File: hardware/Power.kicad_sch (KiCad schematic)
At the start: 0 parts

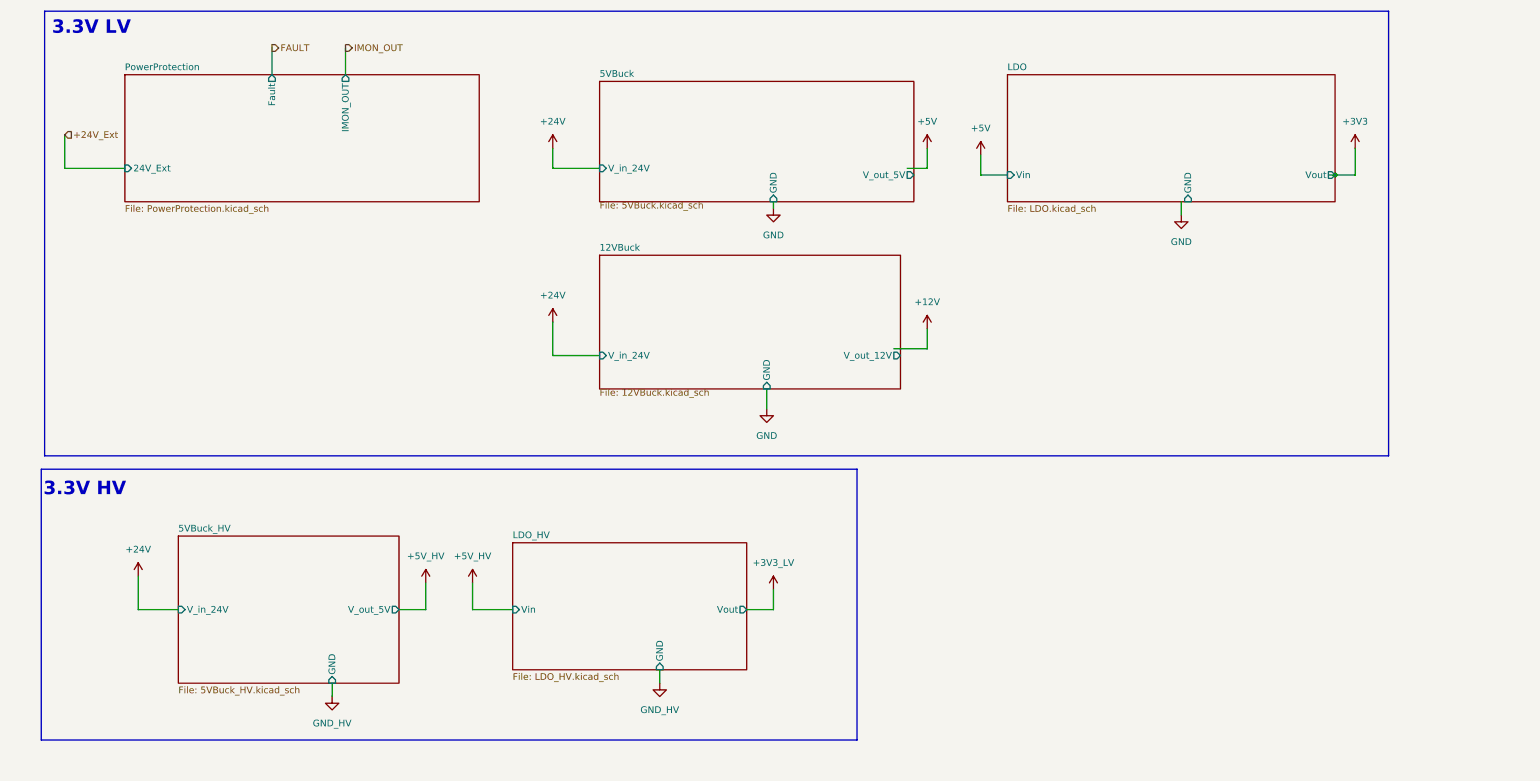
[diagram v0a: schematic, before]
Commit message: added designs for LZSR-80P and AMC class voltage sense
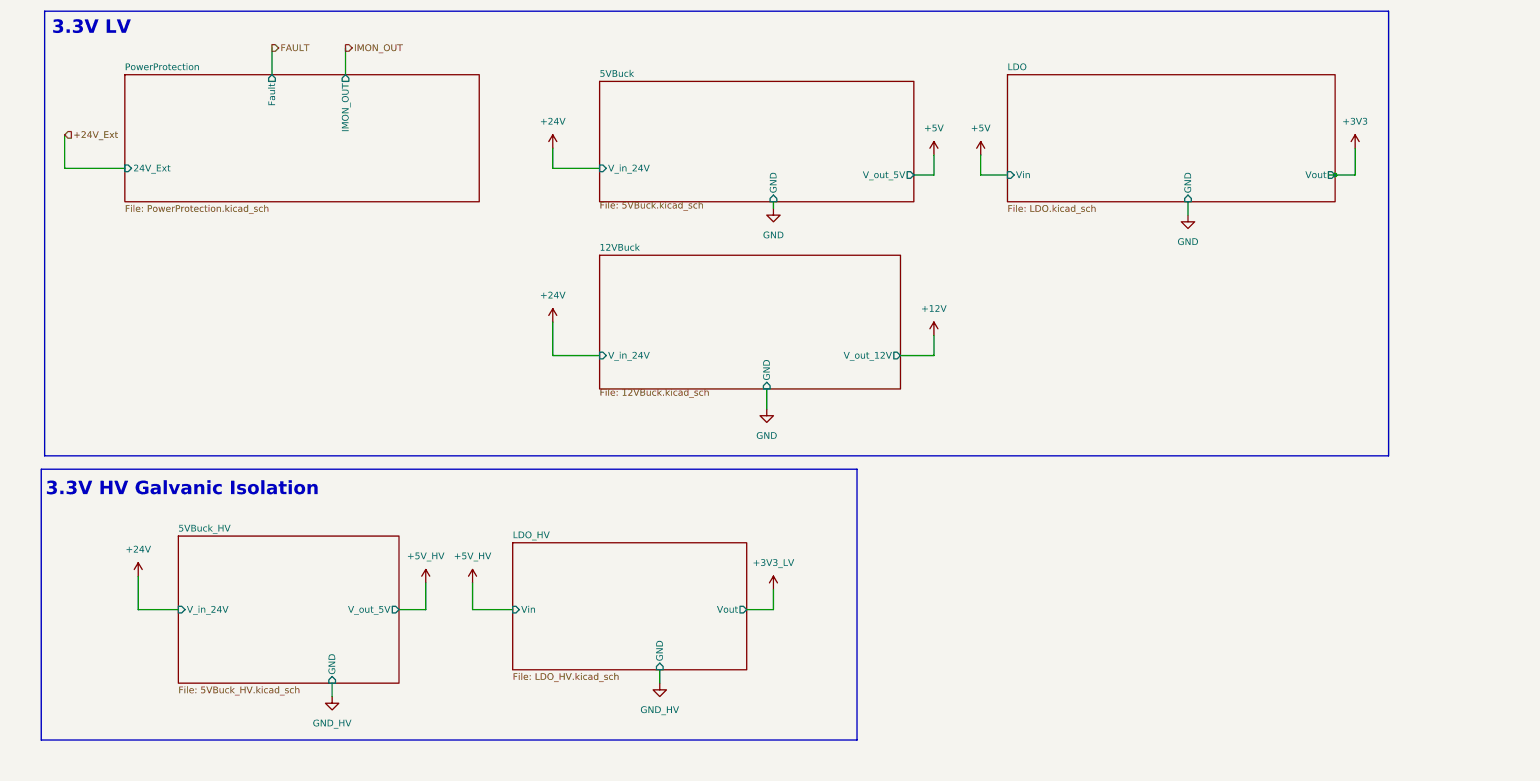
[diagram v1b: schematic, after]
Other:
- note added: "3.3V HV Galvanic Isolation"
- note removed: "3.3V HV"
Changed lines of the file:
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@@
 		)
 	)
-	(text "3.3V HV"
-		(exclude_from_sim no)
-		(at 26.67 109.22 0)
+	(text "3.3V HV Galvanic Isolation\n"
+		(exclude_from_sim no)
+		(at 45.212 109.22 0)
 		(effects
 			(font
@@
 	(wire
 		(pts
-			(xy 180.34 82.55) (xy 186.69 82.55)
+			(xy 181.61 83.82) (xy 187.96 83.82)
 		)
 		(stroke
@@
 	(wire
 		(pts
-			(xy 234.95 57.15) (xy 234.95 54.61)
+			(xy 236.22 57.15) (xy 236.22 54.61)
 		)
 		(stroke
@@
 	(wire
 		(pts
-			(xy 186.69 44.45) (xy 186.69 48.26)
+			(xy 187.96 45.72) (xy 187.96 49.53)
 		)
 		(stroke
@@
 	(wire
 		(pts
-			(xy 186.69 78.74) (xy 186.69 82.55)
+			(xy 187.96 80.01) (xy 187.96 83.82)
 		)
 		(stroke
@@
 	(wire
 		(pts
-			(xy 182.88 48.26) (xy 186.69 48.26)
+			(xy 184.15 49.53) (xy 187.96 49.53)
 		)
 		(stroke
@@
 	(symbol
 		(lib_id "power:+12V")
-		(at 186.69 78.74 0)
+		(at 187.96 80.01 0)
 		(unit 1)
 		(exclude_from_sim no)
@@
 		(fields_autoplaced yes)
 		(property "Reference" "#PWR07"
-			(at 186.69 82.55 0)
+			(at 187.96 83.82 0)
 			(effects
 				(font
@@
 		)
 		(property "Value" "+12V"
-			(at 186.69 73.66 0)
-			(effects
-				(font
-					(size 1.27 1.27)
-				)
-			)
-		)
-		(property "Footprint" ""
-			(at 186.69 78.74 0)
-			(effects
-				(font
-					(size 1.27 1.27)
-				)
-				(hide yes)
-			)
-		)
-		(property "Datasheet" ""
-			(at 186.69 78.74 0)
+			(at 187.96 74.93 0)
+			(effects
+				(font
+					(size 1.27 1.27)
+				)
+			)
+		)
+		(property "Footprint" ""
+			(at 187.96 80.01 0)
+			(effects
+				(font
+					(size 1.27 1.27)
+				)
+				(hide yes)
+			)
+		)
+		(property "Datasheet" ""
+			(at 187.96 80.01 0)
 			(effects
 				(font
@@
 		)
 		(property "Description" "Power symbol creates a global label with name \"+12V\""
-			(at 186.69 78.74 0)
+			(at 187.96 80.01 0)
 			(effects
 				(font
@@
 	(symbol
 		(lib_id "power:+5V")
-		(at 186.69 44.45 0)
+		(at 187.96 45.72 0)
 		(unit 1)
 		(exclude_from_sim no)
@@
 		(fields_autoplaced yes)
 		(property "Reference" "#PWR08"
-			(at 186.69 48.26 0)
+			(at 187.96 49.53 0)
 			(effects
 				(font
@@
 		)
 		(property "Value" "+5V"
-			(at 186.69 39.37 0)
-			(effects
-				(font
-					(size 1.27 1.27)
-				)
-			)
-		)
-		(property "Footprint" ""
-			(at 186.69 44.45 0)
-			(effects
-				(font
-					(size 1.27 1.27)
-				)
-				(hide yes)
-			)
-		)
-		(property "Datasheet" ""
-			(at 186.69 44.45 0)
+			(at 187.96 40.64 0)
+			(effects
+				(font
+					(size 1.27 1.27)
+				)
+			)
+		)
+		(property "Footprint" ""
+			(at 187.96 45.72 0)
+			(effects
+				(font
+					(size 1.27 1.27)
+				)
+				(hide yes)
+			)
+		)
+		(property "Datasheet" ""
+			(at 187.96 45.72 0)
 			(effects
 				(font
@@
 		)
 		(property "Description" "Power symbol creates a global label with name \"+5V\""
-			(at 186.69 44.45 0)
+			(at 187.96 45.72 0)
 			(effects
 				(font
@@
 	(symbol
 		(lib_id "power:GND")
-		(at 234.95 57.15 0)
+		(at 236.22 57.15 0)
 		(unit 1)
 		(exclude_from_sim no)
@@
 		(fields_autoplaced yes)
 		(property "Reference" "#PWR012"
-			(at 234.95 63.5 0)
+			(at 236.22 63.5 0)
 			(effects
 				(font
@@
 		)
 		(property "Value" "GND"
-			(at 234.95 62.23 0)
-			(effects
-				(font
-					(size 1.27 1.27)
-				)
-			)
-		)
-		(property "Footprint" ""
-			(at 234.95 57.15 0)
-			(effects
-				(font
-					(size 1.27 1.27)
-				)
-				(hide yes)
-			)
-		)
-		(property "Datasheet" ""
-			(at 234.95 57.15 0)
+			(at 236.22 62.23 0)
+			(effects
+				(font
+					(size 1.27 1.27)
+				)
+			)
+		)
+		(property "Footprint" ""
+			(at 236.22 57.15 0)
+			(effects
+				(font
+					(size 1.27 1.27)
+				)
+				(hide yes)
+			)
+		)
+		(property "Datasheet" ""
+			(at 236.22 57.15 0)
 			(effects
 				(font
@@
 		)
 		(property "Description" "Power symbol creates a global label with name \"GND\" , ground"
-			(at 234.95 57.15 0)
-			(effects
-				(font
+			(at 236.22 57.15 0)
+			(effects
+				(font

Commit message: labeled + stm32 cube layout
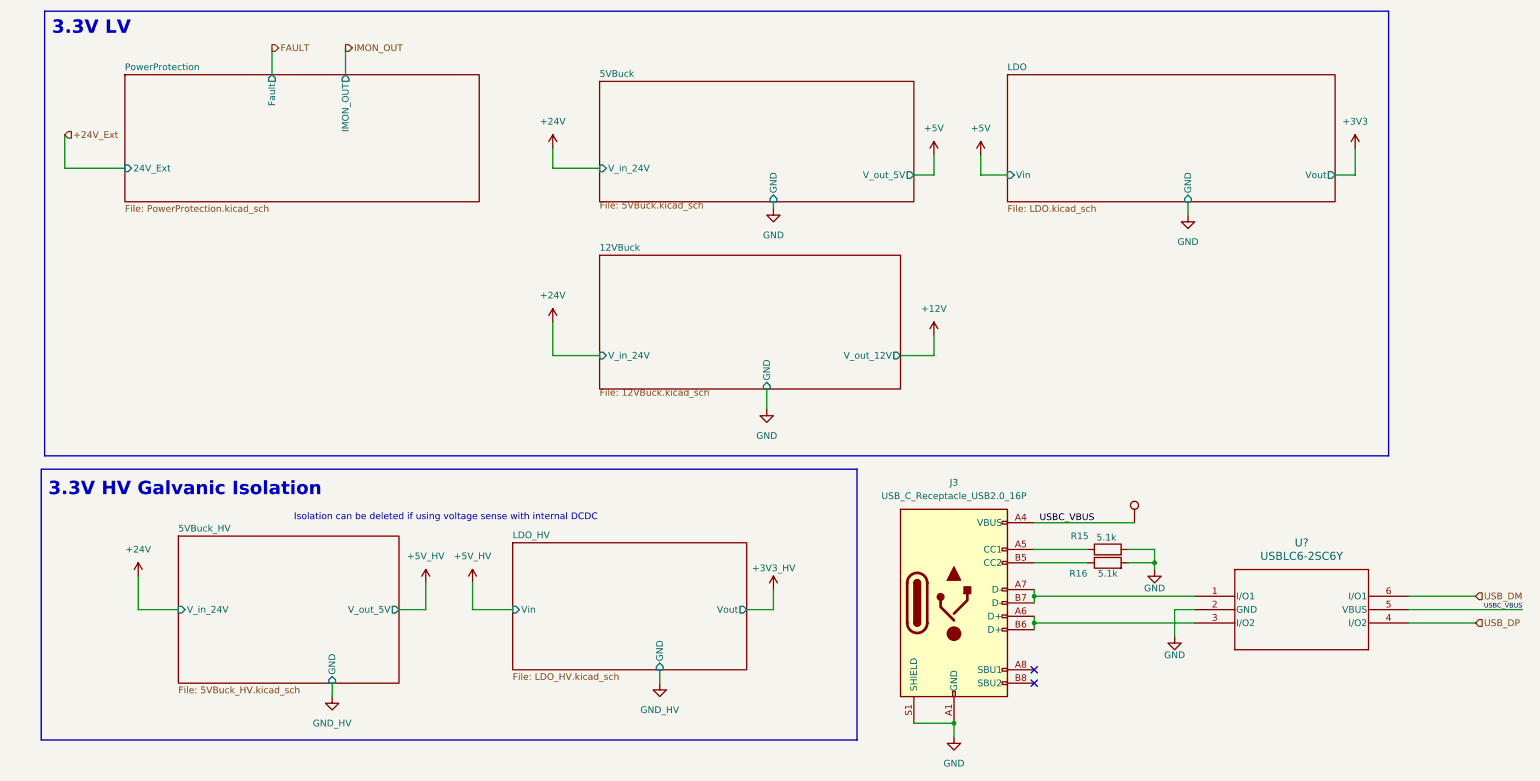
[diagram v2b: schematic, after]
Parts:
- added J3: USB_C_Receptacle_USB2.0_16P, LHRS_ICs:USB_C_Receptacle_GCT_USB4105-xx-A_16P_TopMnt_Horizontal, symbol lhrs_connectors:USB_C_Receptacle_USB2.0_16P
- added R15, R16: 5.1k, symbol Device:R
- added TP?: TestPoint, symbol Connector:TestPoint
- added U?: USBLC6-2SC6Y, SOT23-6L_STM, symbol USBLC6_2SC6Y:USBLC6-2SC6Y
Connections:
- net GND: now also J3.A1 (GND), J3.A12 (GND), J3.B1 (GND), J3.B12 (GND), J3.S1 (SHIELD), J3.S2 (Shield), J3.S3 (Shield), J3.S4 (Shield), R15.2, R16.2, U?.2 (GND)
- new net: J3.A5 (CC1), R15.1
- new net: J3.A7 (D-), J3.B7 (D-), U?.1 (I/O1)
- new net: J3.A6 (D+), J3.B6 (D+), U?.3 (I/O2)
- new net: J3.B5 (CC2), R16.1
- new net USBC_VBUS: J3.A4 (VBUS), J3.A9 (VBUS), J3.B4 (VBUS), J3.B9 (VBUS), TP?.1, U?.5 (VBUS)
- new net USB_DM: U?.6 (I/O1)
- new net USB_DP: U?.4 (I/O2)
- no-connect marks 0 -> 2
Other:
- note added: "Isolation can be deleted if using voltage sense with internal DCDC"

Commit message: added debug led
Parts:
- gave numbers to parts that had none: 2
- renumbered R15 to R22, R16 to R23
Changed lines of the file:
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@@
 		(on_board yes)
 		(dnp no)
-		(property "Reference" "R15"
+		(property "Reference" "R22"
 			(at 215.646 118.11 90)
 			(effects
@@
 			(project ""
 				(path "/2365a867-6254-4a7c-9718-f325e0bbac5c/904fa10a-747c-46cf-90d1-33d76069dc5d"
-					(reference "R15")
+					(reference "R22")
 					(unit 1)
 				)
@@
 		(dnp no)
 		(fields_autoplaced yes)
-		(property "Reference" "#PWR031"
+		(property "Reference" "#PWR038"
 			(at 191.77 162.56 0)
 			(effects
@@
 			(project ""
 				(path "/2365a867-6254-4a7c-9718-f325e0bbac5c/904fa10a-747c-46cf-90d1-33d76069dc5d"
-					(reference "#PWR031")
+					(reference "#PWR038")
 					(unit 1)
 				)
@@
 		(dnp no)
 		(fields_autoplaced yes)
-		(property "Reference" "#PWR019"
+		(property "Reference" "#PWR026"
 			(at 36.83 129.54 0)
 			(effects
@@
 			(project ""
 				(path "/2365a867-6254-4a7c-9718-f325e0bbac5c/904fa10a-747c-46cf-90d1-33d76069dc5d"
-					(reference "#PWR019")
+					(reference "#PWR026")
 					(unit 1)
 				)
@@
 		(on_board yes)
 		(dnp no)
-		(property "Reference" "#PWR079"
+		(property "Reference" "#PWR041"
 			(at 233.68 143.51 0)
 			(effects
@@
 			(project "PS-HVCarrier"
 				(path "/2365a867-6254-4a7c-9718-f325e0bbac5c/904fa10a-747c-46cf-90d1-33d76069dc5d"
-					(reference "#PWR079")
+					(reference "#PWR041")
 					(unit 1)
 				)
@@
 		(dnp no)
 		(fields_autoplaced yes)
-		(property "Reference" "#PWR024"
+		(property "Reference" "#PWR031"
 			(at 115.57 81.28 0)
 			(effects
@@
 			(project ""
 				(path "/2365a867-6254-4a7c-9718-f325e0bbac5c/904fa10a-747c-46cf-90d1-33d76069dc5d"
-					(reference "#PWR024")
+					(reference "#PWR031")
 					(unit 1)
 				)
@@
 		(dnp no)
 		(fields_autoplaced yes)
-		(property "Reference" "#PWR022"
+		(property "Reference" "#PWR029"
 			(at 100.33 130.81 0)
 			(effects
@@
 			(project "PS-HVCarrier"
 				(path "/2365a867-6254-4a7c-9718-f325e0bbac5c/904fa10a-747c-46cf-90d1-33d76069dc5d"
-					(reference "#PWR022")
+					(reference "#PWR029")
 					(unit 1)
 				)
@@
 		(dnp no)
 		(fields_autoplaced yes)
-		(property "Reference" "#PWR025"
+		(property "Reference" "#PWR032"
 			(at 135.89 152.4 0)
 			(effects
@@
 			(project "PS-HVCarrier"
 				(path "/2365a867-6254-4a7c-9718-f325e0bbac5c/904fa10a-747c-46cf-90d1-33d76069dc5d"
-					(reference "#PWR025")
+					(reference "#PWR032")
 					(unit 1)
 				)
@@
 		(dnp no)
 		(fields_autoplaced yes)
-		(property "Reference" "#PWR020"
+		(property "Reference" "#PWR027"
 			(at 73.66 154.94 0)
 			(effects
@@
 			(project ""
 				(path "/2365a867-6254-4a7c-9718-f325e0bbac5c/904fa10a-747c-46cf-90d1-33d76069dc5d"
-					(reference "#PWR020")
+					(reference "#PWR027")
 					(unit 1)
 				)
@@
 		(dnp no)
 		(fields_autoplaced yes)
-		(property "Reference" "#PWR021"
+		(property "Reference" "#PWR028"
 			(at 91.44 130.81 0)
 			(effects
@@
 			(project ""
 				(path "/2365a867-6254-4a7c-9718-f325e0bbac5c/904fa10a-747c-46cf-90d1-33d76069dc5d"
-					(reference "#PWR021")
+					(reference "#PWR028")
 					(unit 1)
 				)
@@
 		(dnp no)
 		(fields_autoplaced yes)
-		(property "Reference" "U?"
+		(property "Reference" "U5"
 			(at 257.81 119.38 0)
 			(effects
@@
 			(project ""
 				(path "/2365a867-6254-4a7c-9718-f325e0bbac5c/904fa10a-747c-46cf-90d1-33d76069dc5d"
-					(reference "U?")
+					(reference "U5")
 					(unit 1)
 				)
@@
 		(dnp no)
 		(fields_autoplaced yes)
-		(property "Reference" "#PWR030"
+		(property "Reference" "#PWR037"
 			(at 187.96 83.82 0)
 			(effects
@@
 			(project ""
 				(path "/2365a867-6254-4a7c-9718-f325e0bbac5c/904fa10a-747c-46cf-90d1-33d76069dc5d"
-					(reference "#PWR030")
+					(reference "#PWR037")
 					(unit 1)
 				)
@@
 		(dnp no)
 		(fields_autoplaced yes)
-		(property "Reference" "#PWR032"
+		(property "Reference" "#PWR039"
 			(at 196.85 49.53 0)
 			(effects
@@
 			(project "PS-HVCarrier"
 				(path "/2365a867-6254-4a7c-9718-f325e0bbac5c/904fa10a-747c-46cf-90d1-33d76069dc5d"
-					(reference "#PWR032")
+					(reference "#PWR039")
 					(unit 1)
 				)
@@
 		(dnp no)
 		(fields_autoplaced yes)
-		(property "Reference" "#PWR035"
+		(property "Reference" "#PWR043"
 			(at 267.97 48.26 0)
 			(effects
@@
 			(project ""
 				(path "/2365a867-6254-4a7c-9718-f325e0bbac5c/904fa10a-747c-46cf-90d1-33d76069dc5d"
-					(reference "#PWR035")
+					(reference "#PWR043")
 					(unit 1)
 				)
@@
 		(dnp no)
 		(fields_autoplaced yes)
-		(property "Reference" "#PWR029"
+		(property "Reference" "#PWR036"
 			(at 187.96 49.53 0)
 			(effects
@@
 			(project ""
 				(path "/2365a867-6254-4a7c-9718-f325e0bbac5c/904fa10a-747c-46cf-90d1-33d76069dc5d"
-					(reference "#PWR029")
+					(reference "#PWR036")
 					(unit 1)
 				)
@@
 		(dnp no)
 		(fields_autoplaced yes)
-		(property "Reference" "TP?"
+		(property "Reference" "TP19"
 			(at 228.6 110.9979 0)
 			(effects
@@
 			(project ""
 				(path "/2365a867-6254-4a7c-9718-f325e0bbac5c/904fa10a-747c-46cf-90d1-33d76069dc5d"
-					(reference "TP?")
+					(reference "TP19")
 					(unit 1)
 				)
@@
 		(on_board yes)
 		(dnp no)
-		(property "Reference" "#PWR028"
+		(property "Reference" "#PWR035"
 			(at 157.48 132.08 0)
 			(effects
@@
 			(project ""
 				(path "/2365a867-6254-4a7c-9718-f325e0bbac5c/904fa10a-747c-46cf-90d1-33d76069dc5d"
-					(reference "#PWR028")
+					(reference "#PWR035")
 					(unit 1)
 				)
@@
 		(on_board yes)
 		(dnp no)
-		(property "Reference" "#PWR033"
+		(property "Reference" "#PWR040"
 			(at 229.87 130.81 0)
 			(effects
@@
 			(project ""
 				(path "/2365a867-6254-4a7c-9718-f325e0bbac5c/904fa10a-747c-46cf-90d1-33d76069dc5d"
-					(reference "#PWR033")
+					(reference "#PWR040")
 					(unit 1)
 				)
@@
 		(dnp no)
 		(fields_autoplaced yes)
-		(property "Reference" "#PWR026"
+		(property "Reference" "#PWR033"
 			(at 156.21 100.33 0)
 			(effects
@@
 			(project "PS-HVCarrier"
 				(path "/2365a867-6254-4a7c-9718-f325e0bbac5c/904fa10a-747c-46cf-90d1-33d76069dc5d"
-					(reference "#PWR026")
+					(reference "#PWR033")
 					(unit 1)
 				)
@@
 		(dnp no)
 		(fields_autoplaced yes)
-		(property "Reference" "#PWR027"
+		(property "Reference" "#PWR034"
 			(at 157.48 62.23 0)
 			(effects
@@
 			(project ""
 				(path "/2365a867-6254-4a7c-9718-f325e0bbac5c/904fa10a-747c-46cf-90d1-33d76069dc5d"
-					(reference "#PWR027")
+					(reference "#PWR034")
 					(unit 1)
 				)
@@
 		(dnp no)
 		(fields_autoplaced yes)
-		(property "Reference" "#PWR034"
+		(property "Reference" "#PWR042"
 			(at 236.22 63.5 0)
 			(effects
@@
 			(project "PS-HVCarrier"
 				(path "/2365a867-6254-4a7c-9718-f325e0bbac5c/904fa10a-747c-46cf-90d1-33d76069dc5d"
-					(reference "#PWR034")
+					(reference "#PWR042")
 					(unit 1)
 				)
@@
 		(dnp no)
 		(fields_autoplaced yes)
-		(property "Reference" "#PWR023"
+		(property "Reference" "#PWR030"
 			(at 115.57 48.26 0)
 			(effects
@@
 			(project ""
 				(path "/2365a867-6254-4a7c-9718-f325e0bbac5c/904fa10a-747c-46cf-90d1-33d76069dc5d"
-					(reference "#PWR023")
+					(reference "#PWR030")
 					(unit 1)
 				)
@@
 		(on_board yes)
 		(dnp no)
-		(property "Reference" "R16"
+		(property "Reference" "R23"
 			(at 215.392 125.222 90)
 			(effects
@@
 			(project "PS-HVCarrier"
 				(path "/2365a867-6254-4a7c-9718-f325e0bbac5c/904fa10a-747c-46cf-90d1-33d76069dc5d"
-					(reference "R16")
-					(unit 1)
-				)
+					(reference "R23")
+					(unit 1)
+				)
